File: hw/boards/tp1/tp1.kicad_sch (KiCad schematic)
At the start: 17 parts, among them J1 Conn_01x20, J2 Conn_01x20, J3 BC-1-208, J4 BC-1-701, Q1 AO3400A, Q2 AO3401A, U2 Pico

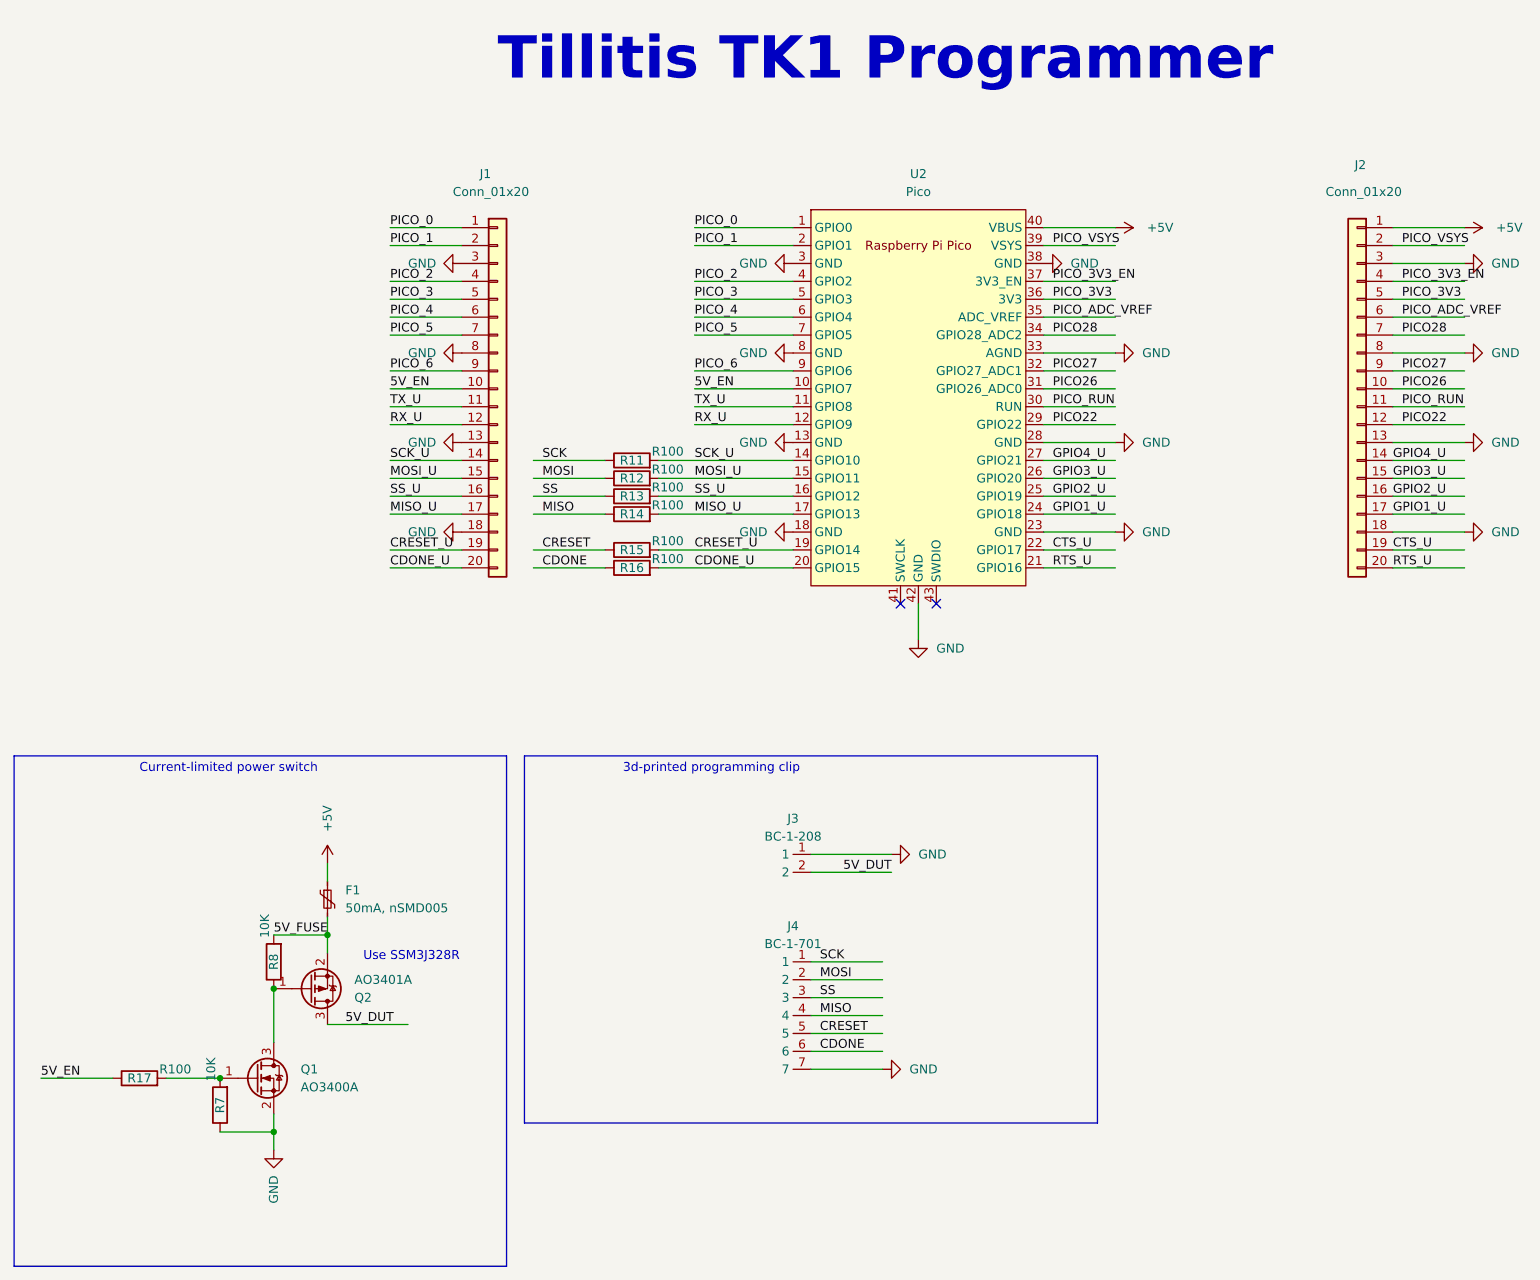
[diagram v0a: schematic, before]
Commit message: Fixes for production programmer PCB
* Swap GND and 5V on J3
* Replace graphic logo with text
* Rename part to 'TP-1'
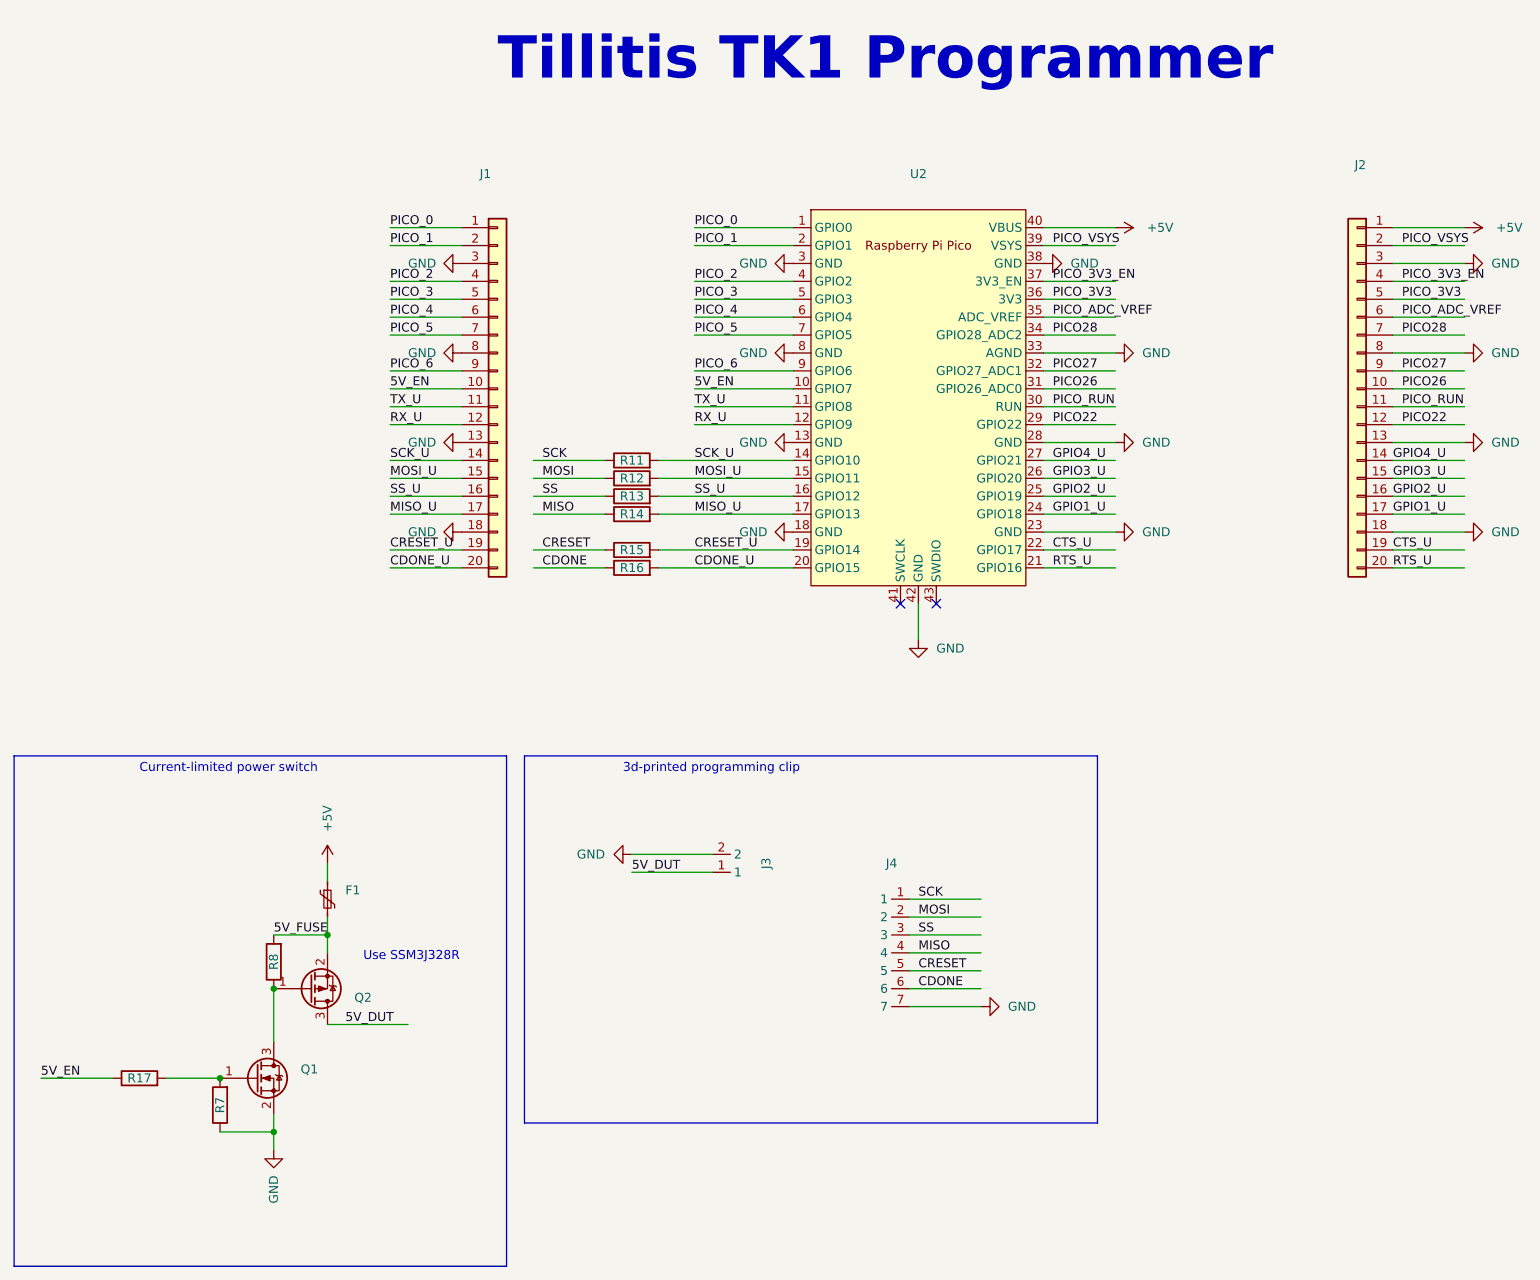
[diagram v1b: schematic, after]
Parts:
- F1: value 50mA, nSMD005 -> (none); footprint Fuse:Fuse_1206_3216Metric -> (none); Manufacturer (none) -> Bel Fuse; Manufacturer Part Number (none) -> 0ZCJ0005FF2E; Supplier (none) -> Digikey; Supplier Part Number (none) -> 507-1793-2-ND
- J1, J2: value Conn_01x20 -> (none); footprint Connector_PinHeader_2.54mm:PinHeader_1x20_P2.54mm_Vertical -> (none); now left out of the parts list
- J3: value BC-1-208 -> (none); footprint mta1:BC-1-208 -> (none); Manufacturer (none) -> Disong; Manufacturer Part Number (none) -> BC-1-208
- J4: value BC-1-701 -> (none); footprint mta1:BC-1-701 -> (none); Manufacturer (none) -> Disong; Manufacturer Part Number (none) -> BC-1-701
- Q1: value AO3400A -> (none); footprint Package_TO_SOT_SMD:SOT-23 -> (none)
- Q2: value AO3401A -> (none); footprint Package_TO_SOT_SMD:SOT-23 -> (none)
- R11, R12, R13, R14, R15, R16, R17: value R100 -> (none); footprint mta1:ERJ2G(0402)_L -> (none); Extended Value (none) -> 1/16W,5%; Manufacturer (none) -> Any/not critical
- R7, R8: value 10K -> (none); footprint mta1:ERJ2G(0402)_L -> (none); Extended Value (none) -> 1/16W,5%; Manufacturer (none) -> Any/not critical
- U2: value Pico -> (none); footprint MCU_RaspberryPi_and_Boards:RPi_Pico_SMD -> (none); Manufacturer (none) -> Raspberry Pi; Manufacturer Part Number (none) -> SC0915; Supplier (none) -> Digikey; Supplier Part Number (none) -> 2648-SC0915TR-ND
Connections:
- net 5V_DUT: now also J3.1; no longer J3.2
- net GND: now also J3.2; no longer J3.1
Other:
- moved on the sheet: J3, J4
